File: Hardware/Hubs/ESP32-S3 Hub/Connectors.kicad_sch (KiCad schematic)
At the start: 25 parts, among them J1 1.27mm 3pin socket, J10 1.27mm 3pin socket, J11 7 pin FPC 0.3mm Panasonic Y3b, J12 1.27mm 3pin socket, J13 TE 3-2363961-0 receptacle, J14 TE 3-2363962-0 Connector, J16 TE 3-2363961-0 receptacle, J17 TE 3-2363962-0 Connector, J2 1.27mm 3pin socket, J21 1.27mm 4 pin socket, J22 1.27mm 4 pin header, J3 7 pin FPC 0.3mm Panasonic Y3b, J4 1.27mm 3pin socket, J5 7 pin FPC 0.3mm Panasonic Y3b, J6 1.27mm 3pin socket, J7 1.27mm 3pin socket, J8 7 pin FPC 0.3mm Panasonic Y3b, J9 1.27mm 3pin socket

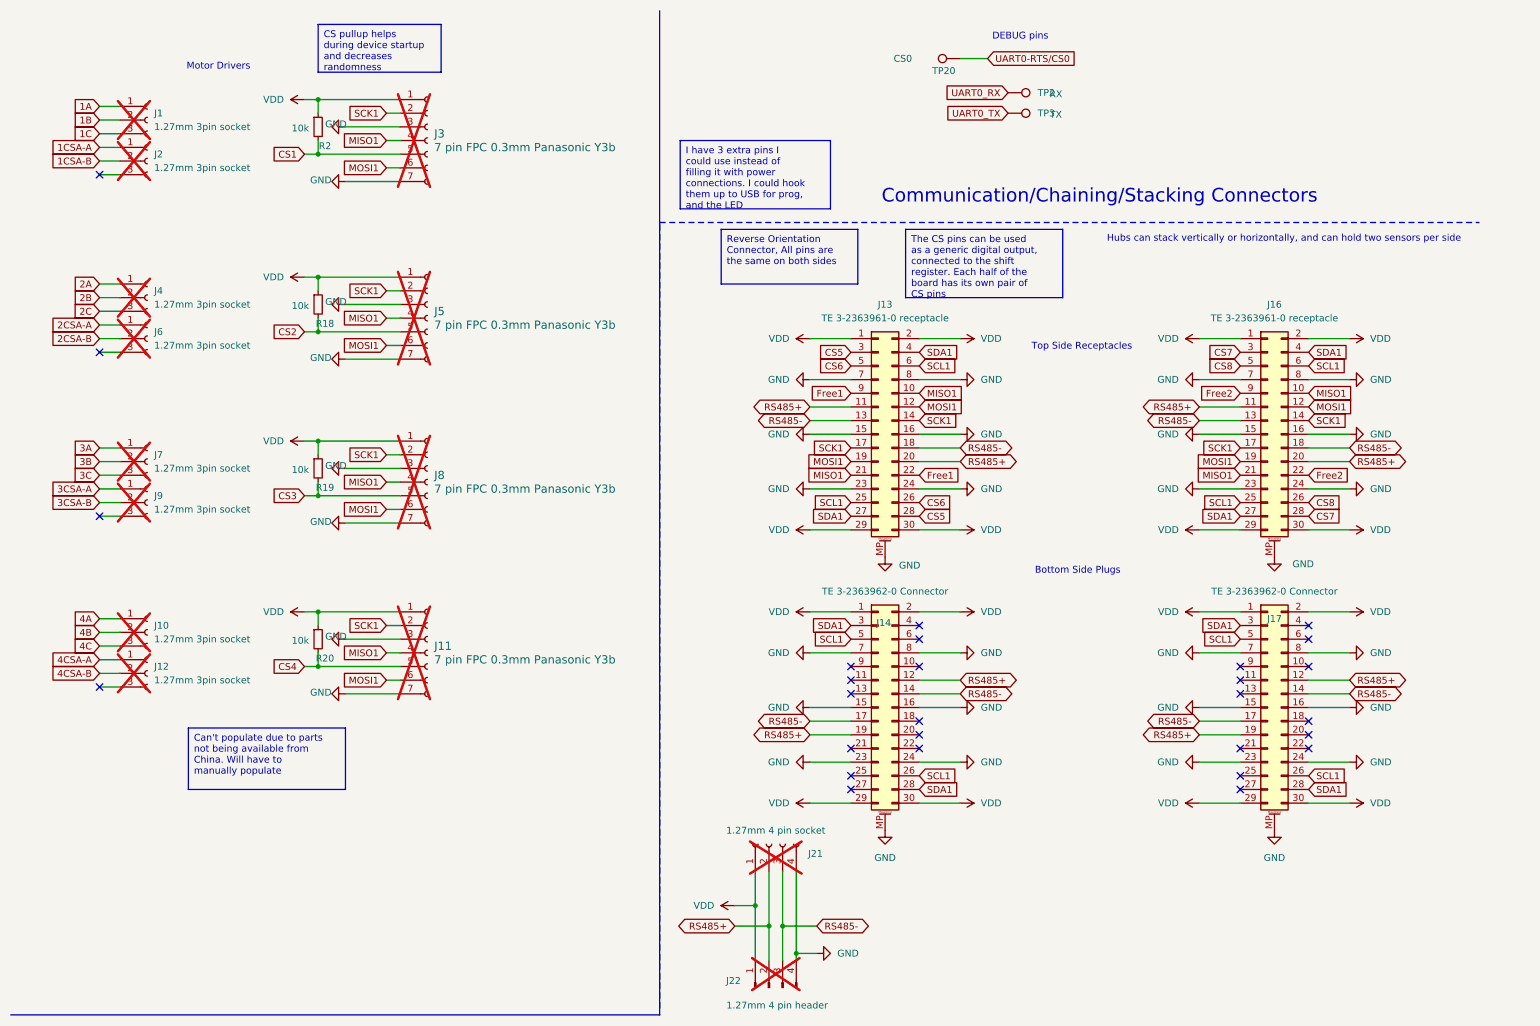
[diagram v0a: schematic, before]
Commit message: Updated connectors in schem and pcb
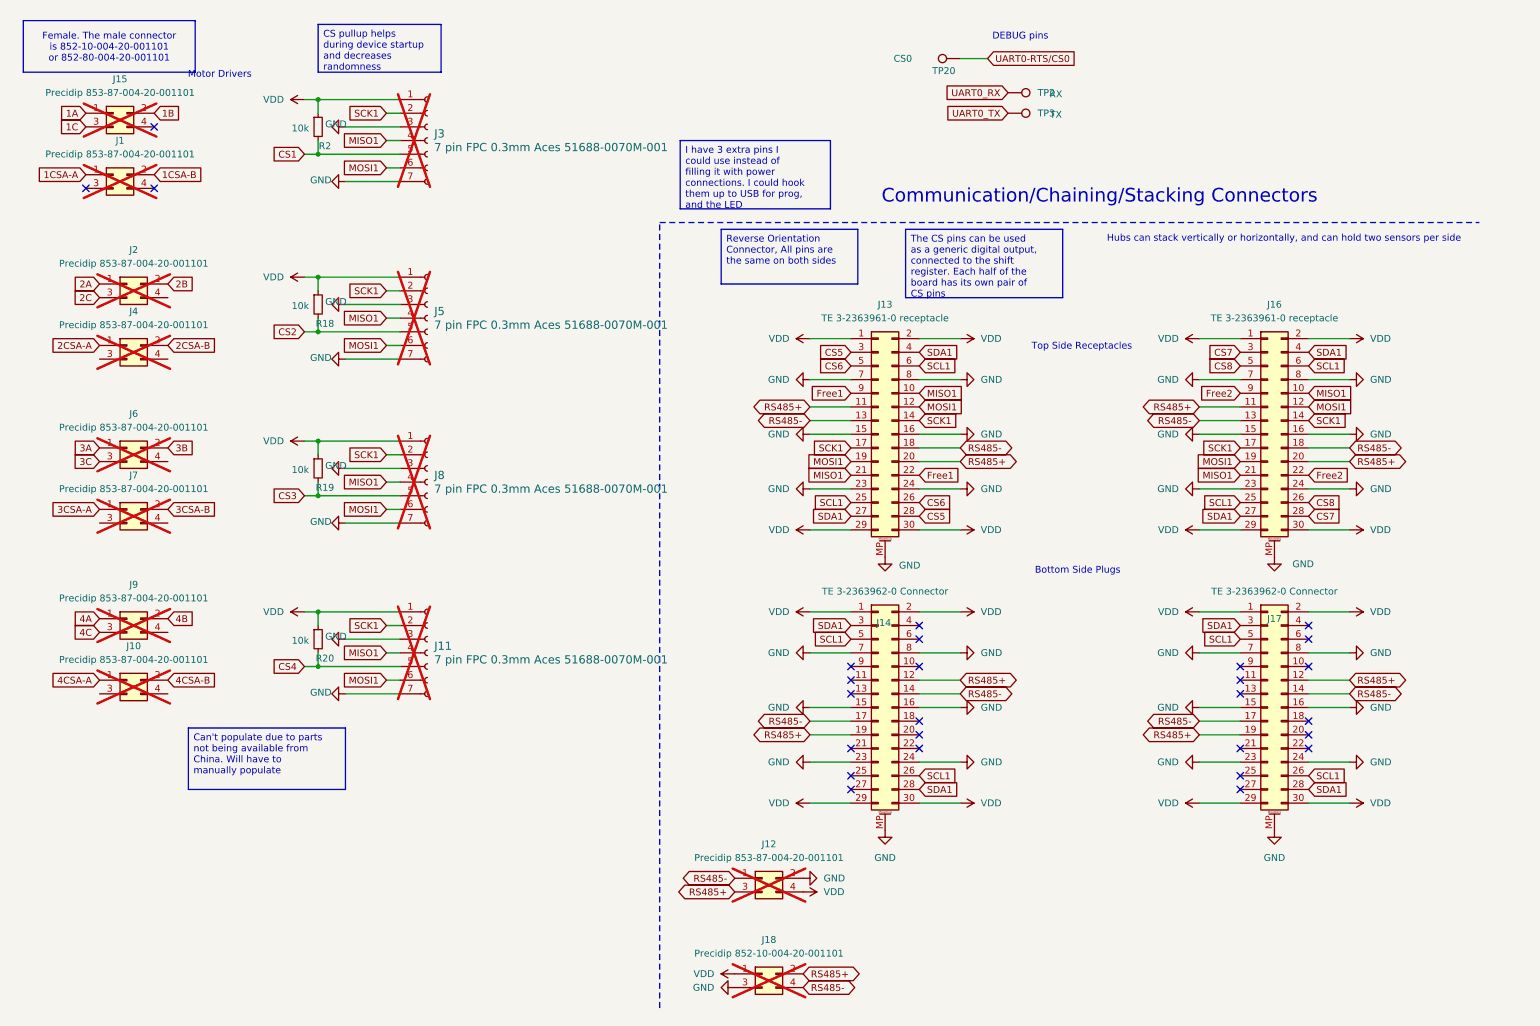
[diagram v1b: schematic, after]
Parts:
- removed J1, J10, J12, J2, J4, J6, J7, J9: 1.27mm 3pin socket, Connector_PinHeader_1.27mm:PinHeader_1x03_P1.27mm_Vertical, symbol Connector:Conn_01x03_Socket
- removed J21: 1.27mm 4 pin socket, Connector_PinSocket_1.27mm:PinSocket_1x04_P1.27mm_Vertical, symbol Connector:Conn_01x04_Socket
- removed J22: 1.27mm 4 pin header, Connector_PinHeader_1.27mm:PinHeader_1x04_P1.27mm_Horizontal, symbol Connector:Conn_01x04_Pin
- added J1, J10, J12, J15, J2, J4, J6, J7, J9: Precidip 853-87-004-20-001101, Connector_PinHeader_1.27mm:PinHeader_2x02_P1.27mm_Horizontal, symbol Connector_Generic:Conn_02x02_Odd_Even
- added J18: Precidip 852-10-004-20-001101, Connector_PinHeader_1.27mm:PinHeader_2x02_P1.27mm_Horizontal, symbol Connector_Generic:Conn_02x02_Odd_Even
- J11, J3, J5, J8: value 7 pin FPC 0.3mm Panasonic Y3b -> 7 pin FPC 0.3mm Aces 51688-0070M-001; footprint custom_Interface_HID:fpc_7pin_0.3mm_connector Panasonic -> custom_Connector:fpc_7pin_0.3mm_connector Aces
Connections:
- net 1A: now also J15.1 (Pin_1)
- net 1B: now also J15.2 (Pin_2)
- net 1C: now also J15.3 (Pin_3)
- net 1CSA-A: now also J1.1 (Pin_1)
- net 1CSA-B: now also J1.2 (Pin_2)
- net 2A: now also J2.1 (Pin_1)
- net 2B: now also J2.2 (Pin_2)
- net 2C: now also J2.3 (Pin_3)
- net 2CSA-A: now also J4.1 (Pin_1)
- net 2CSA-B: now also J4.2 (Pin_2)
- net 3A: now also J6.1 (Pin_1)
- net 3B: now also J6.2 (Pin_2)
- net 3C: now also J6.3 (Pin_3)
- net 3CSA-A: now also J7.1 (Pin_1)
- net 3CSA-B: now also J7.2 (Pin_2)
- net 4A: now also J9.1 (Pin_1)
- net 4B: now also J9.2 (Pin_2)
- net 4C: now also J9.3 (Pin_3)
- net 4CSA-A: now also J10.1 (Pin_1)
- net 4CSA-B: now also J10.2 (Pin_2)
- net GND: now also J12.2 (Pin_2), J18.3 (Pin_3)
- net RS485+: now also J12.3 (Pin_3), J18.2 (Pin_2)
- net RS485-: now also J12.1 (Pin_1), J18.4 (Pin_4)
- net VDD: now also J12.4 (Pin_4), J18.1 (Pin_1)
- no-connect marks 28 -> 27
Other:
- title: CACKLE -  Hub/Connectors -> CACKLE -  Hub

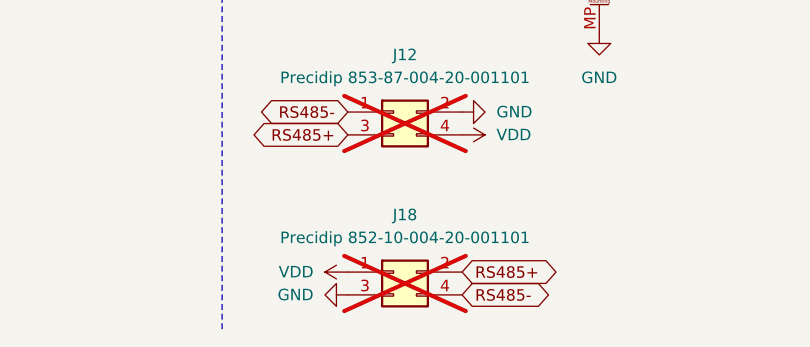
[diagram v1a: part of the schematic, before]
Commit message: Updated component arrangements and fixed pinout on upstream port
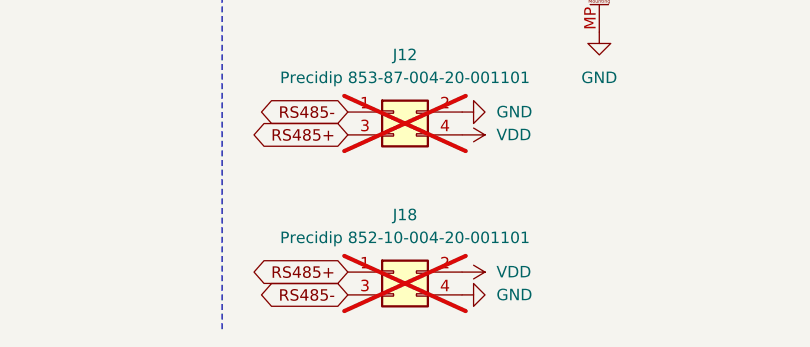
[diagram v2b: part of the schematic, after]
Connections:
- net GND: now also J18.4 (Pin_4); no longer J18.3 (Pin_3)
- net RS485+: now also J18.1 (Pin_1); no longer J18.2 (Pin_2)
- net RS485-: now also J18.3 (Pin_3); no longer J18.4 (Pin_4)
- net VDD: now also J18.2 (Pin_2); no longer J18.1 (Pin_1)
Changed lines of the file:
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@@
 	(global_label "RS485-"
 		(shape bidirectional)
-		(at 160.02 194.31 0)
+		(at 147.32 194.31 180)
 		(fields_autoplaced yes)
 		(effects
@@
 				(size 1.27 1.27)
 			)
-			(justify left)
+			(justify right)
 		)
 		(property "Intersheetrefs" "${INTERSHEET_REFS}"
-			(at 171.7969 194.31 0)
+			(at 135.5431 194.31 0)
 			(effects
 				(font
 					(size 1.27 1.27)
 				)
-				(justify left)
+				(justify right)
 				(hide yes)
 			)
@@
 	(global_label "RS485+"
 		(shape bidirectional)
-		(at 160.02 191.77 0)
+		(at 147.32 191.77 180)
 		(fields_autoplaced yes)
 		(effects
@@
 				(size 1.27 1.27)
 			)
-			(justify left)
+			(justify right)
 		)
 		(property "Intersheetrefs" "${INTERSHEET_REFS}"
-			(at 171.7969 191.77 0)
+			(at 135.5431 191.77 0)
 			(effects
 				(font
 					(size 1.27 1.27)
 				)
-				(justify left)
+				(justify right)
 				(hide yes)
 			)
@@
 	(symbol
 		(lib_id "power:GND")
-		(at 147.32 194.31 270)
+		(at 160.02 194.31 90)
+		(mirror x)
 		(unit 1)
 		(exclude_from_sim no)
@@
 		(fields_autoplaced yes)
 		(property "Reference" "#PWR080"
-			(at 140.97 194.31 0)
+			(at 166.37 194.31 0)
 			(effects
 				(font
@@
 		)
 		(property "Value" "GND"
-			(at 143.51 194.3099 90)
+			(at 163.83 194.3099 90)
 			(effects
 				(font
@@
 		)
 		(property "Footprint" ""
-			(at 147.32 194.31 0)
+			(at 160.02 194.31 0)
 			(effects
 				(font
@@
 		)
 		(property "Datasheet" ""
-			(at 147.32 194.31 0)
+			(at 160.02 194.31 0)
 			(effects
 				(font
@@
 		)
 		(property "Description" "Power symbol creates a global label with name \"GND\" , ground"
-			(at 147.32 194.31 0)
+			(at 160.02 194.31 0)
 			(effects
 				(font
@@
 	(symbol
 		(lib_id "power:VDD")
-		(at 147.32 191.77 90)
+		(at 160.02 191.77 270)
+		(mirror x)
 		(unit 1)
 		(exclude_from_sim no)
@@
 		(fields_autoplaced yes)
 		(property "Reference" "#PWR081"
-			(at 151.13 191.77 0)
+			(at 156.21 191.77 0)
 			(effects
 				(font
@@
 		)
 		(property "Value" "VDD"
-			(at 143.51 191.7699 90)
+			(at 163.83 191.7699 90)
 			(effects
 				(font
@@
 		)
 		(property "Footprint" ""
-			(at 147.32 191.77 0)
+			(at 160.02 191.77 0)
 			(effects
 				(font
@@
 		)
 		(property "Datasheet" ""
-			(at 147.32 191.77 0)
+			(at 160.02 191.77 0)
 			(effects
 				(font
@@
 		)
 		(property "Description" "Power symbol creates a global label with name \"VDD\""
-			(at 147.32 191.77 0)
+			(at 160.02 191.77 0)
 			(effects
 				(font

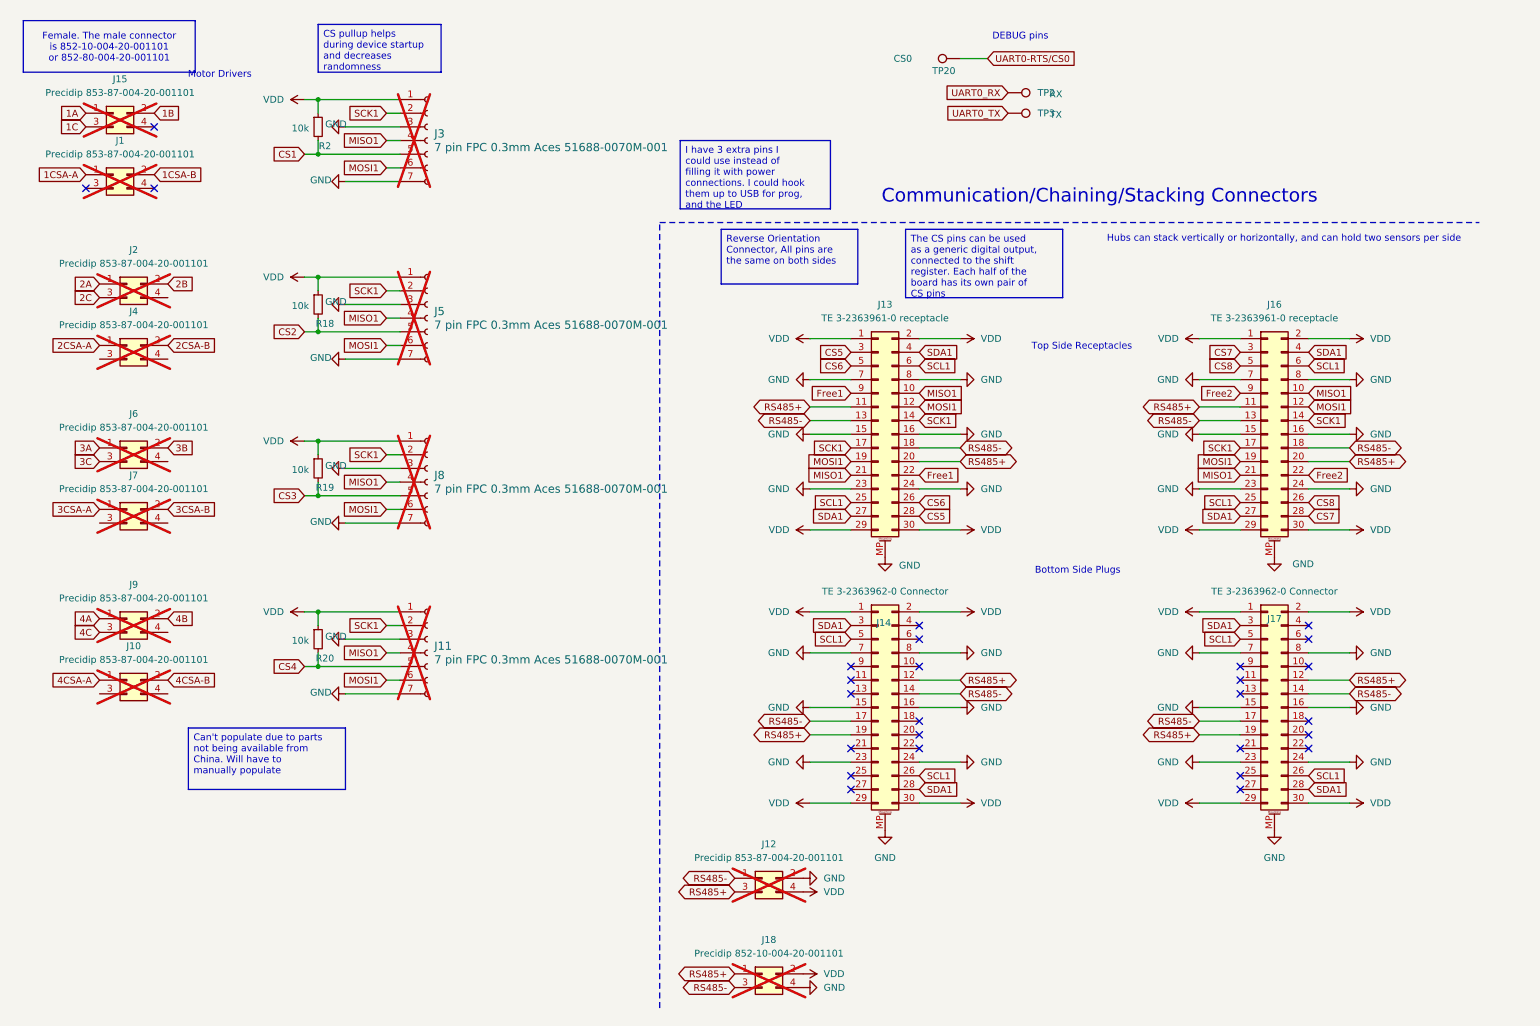
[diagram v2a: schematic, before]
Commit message: Removed bottom side connectors due to infeasability for expansion
Only 4 port mcu hubs could have the double sided expansion unless the MCU was a BGA stuffed away in a corner, so it wouldn't be a common feature. Also it adds a ton of complexity for the RS r485 lines to communicate with an MCU via split wires.
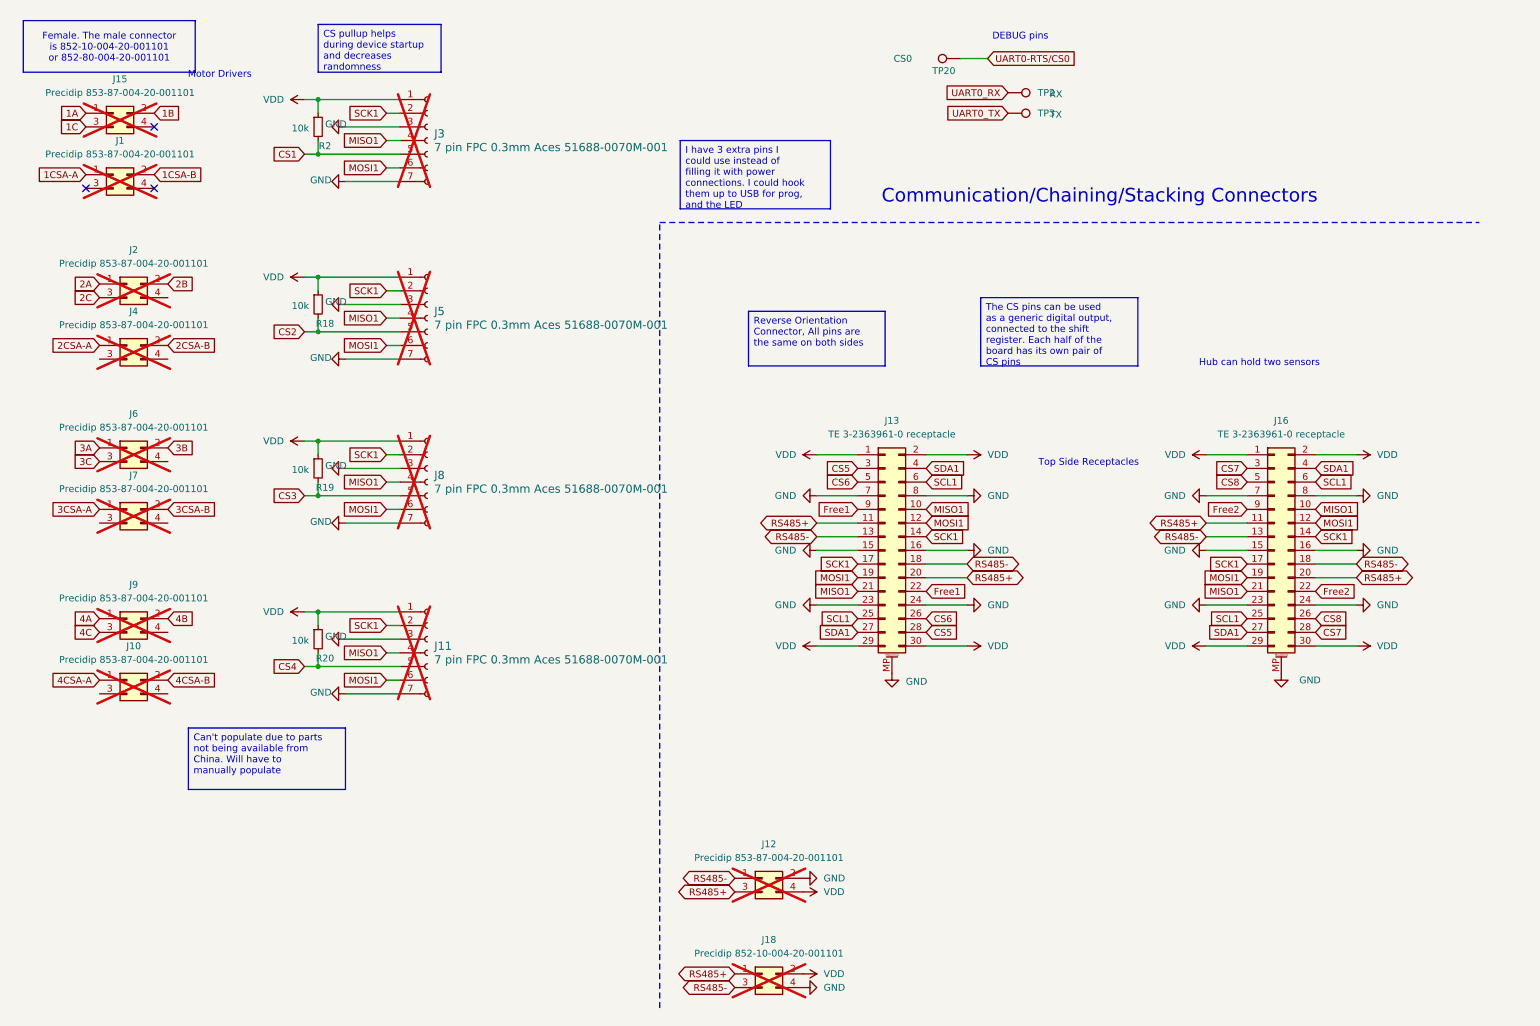
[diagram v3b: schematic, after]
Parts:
- removed J14, J17: TE 3-2363962-0 Connector, custom_testpoints:TE_mezzanine_conn_3-2363962-0, symbol Connector_Generic_MountingPin:Conn_02x15_Odd_Even_MountingPin
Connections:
- no-connect marks 27 -> 3
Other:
- note added: "Hub can hold two sensors"
- note removed: "Bottom Side Plugs"
- note removed: "Hubs can stack vertically or horizontally, and can hold two sensors per side"
- moved on the sheet: J13, J16
